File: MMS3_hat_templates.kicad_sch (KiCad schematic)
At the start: 10 parts

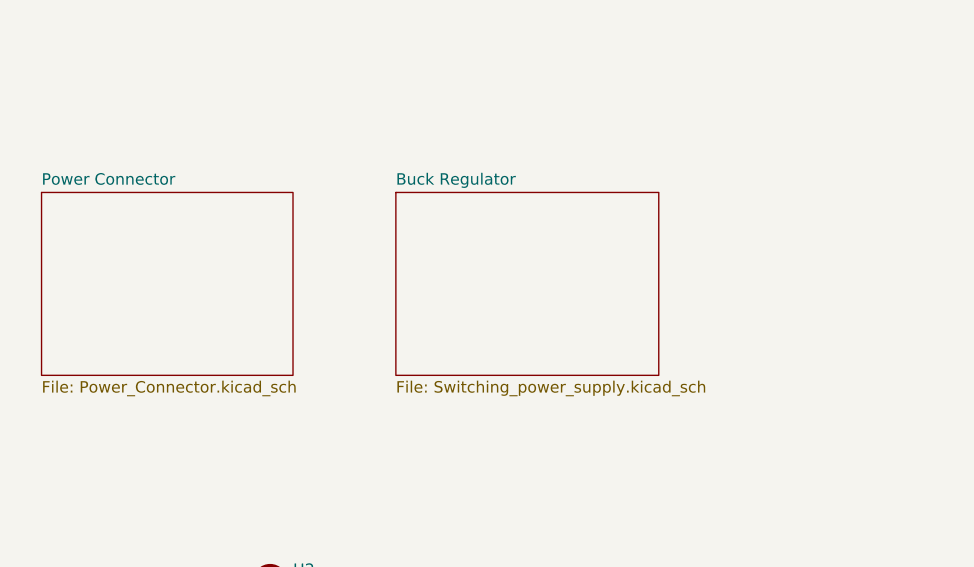
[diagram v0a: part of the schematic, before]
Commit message: template board cleansed
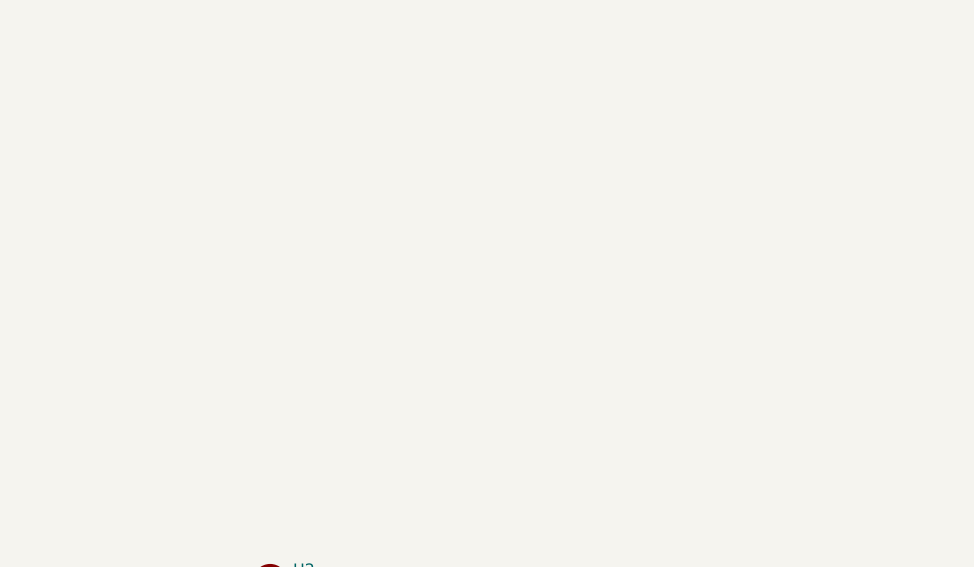
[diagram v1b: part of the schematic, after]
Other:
- removed sheet Buck Regulator
- removed sheet Power Connector
